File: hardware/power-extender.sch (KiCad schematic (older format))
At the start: 8 parts, among them J5 Conn_01x04_Male, J6 Conn_01x04_Male, U10 ADS1115IDGS, U9 ADS1115IDGS

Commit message: First draft
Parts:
- removed J5: Conn_01x04_Male, Connector_JST:JST_XH_B4B-XH-A_1x04_P2.50mm_Vertical, symbol Connector:Conn_01x04_Male
- added J5: RPI IFACE, Connector_JST:JST_XH_B5B-XH-A_1x05_P2.50mm_Vertical, symbol Connector:Conn_01x05_Male
- added J7: AUX DIGITAL, Connector_PinHeader_2.54mm:PinHeader_1x04_P2.54mm_Vertical, symbol Connector:Conn_01x04_Male
- added Q5, Q6: BSS138, Package_TO_SOT_SMD:SOT-23, symbol Transistor_FET:BSS138
- added R19: 1K, Resistor_SMD:R_0805_2012Metric, symbol Device:R
- added R20, R21: 10K, Resistor_SMD:R_0805_2012Metric, symbol Device:R
- added U11: PCA9557PW, Package_SO:TSSOP-16_4.4x5mm_P0.65mm, symbol CustomComponents:PCA9557PW
- C10, C9: footprint Capacitor_SMD:C_0201_0603Metric -> Capacitor_SMD:C_0805_2012Metric
- J6: value Conn_01x04_Male -> AUX ANALOG
- R17, R18: footprint Resistor_SMD:R_0201_0603Metric -> Resistor_SMD:R_0805_2012Metric
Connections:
- net labels added: +3V3, +5V, D0Z, D1, D2, D3
- net labels removed: VCC
- wire segments 36 -> 76
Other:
- note added: "ADDR: 0011000"
- note added: "Additional Analog Inputs"
- note added: "Low-Power Interfaces\nI2C Level Shifter"
- note added: "Relay Subsystem"
- moved on the sheet: C10, C9, J6, U10, U9

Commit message: Firnish schematic first version
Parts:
- added H1, H2, H3, H4: MountingHole, MountingHole:MountingHole_3.2mm_M3, symbol Mechanical:MountingHole
- added J8: IFACE PASS, Connector_JST:JST_XH_B5B-XH-A_1x05_P2.50mm_Vertical, symbol Connector:Conn_01x05_Male
- J5: value RPI IFACE -> IFACE RPI
- J6, J7: footprint Connector_PinHeader_2.54mm:PinHeader_1x04_P2.54mm_Vertical -> Connector_JST:JST_XH_B4B-XH-A_1x04_P2.50mm_Vertical
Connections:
- net +3V3: now also J8.2 (Pin_2)
- net +5V: now also J8.1 (Pin_1)
- net GND: now also J8.5 (Pin_5)
- net SDA3V3: now reaches J5.3 (Pin_3), Q5.2 (S), R17.2
- net SDA3V3: now also J8.3 (Pin_3)
- net SCL3V3: now reaches J5.4 (Pin_4), Q6.2 (S), R18.2
- net SCL3V3: now also J8.4 (Pin_4)
- net SCL renamed SCL5V
- net SDA renamed SDA5V
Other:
- moved on the sheet: C10, C9, J5, J6, J7, Q5, Q6, R17, R18, R19, R20, R21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

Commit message: checkpoint commit
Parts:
- added FID1, FID2, FID3: Fiducial, Fiducial:Fiducial_1mm_Mask2mm, symbol Mechanical:Fiducial
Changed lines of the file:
@@
 Wire Notes Line
 	8950 3300 8950 6000
+$Comp
+L Mechanical:Fiducial FID1
+U 1 1 60E092A2
+P 8350 2250
+F 0 "FID1" H 8435 2296 50  0000 L CNN
+F 1 "Fiducial" H 8435 2205 50  0000 L CNN
+F 2 "Fiducial:Fiducial_1mm_Mask2mm" H 8350 2250 50  0001 C CNN
+F 3 "~" H 8350 2250 50  0001 C CNN
+	1    8350 2250
+	1    0    0    -1
+$EndComp
+$Comp
+L Mechanical:Fiducial FID2
+U 1 1 60E0A4F4
+P 8350 2500
+F 0 "FID2" H 8435 2546 50  0000 L CNN
+F 1 "Fiducial" H 8435 2455 50  0000 L CNN
+F 2 "Fiducial:Fiducial_1mm_Mask2mm" H 8350 2500 50  0001 C CNN
+F 3 "~" H 8350 2500 50  0001 C CNN
+	1    8350 2500
+	1    0    0    -1
+$EndComp
+$Comp
+L Mechanical:Fiducial FID3
+U 1 1 60E11CA0
+P 8350 2750
+F 0 "FID3" H 8435 2796 50  0000 L CNN
+F 1 "Fiducial" H 8435 2705 50  0000 L CNN
+F 2 "Fiducial:Fiducial_1mm_Mask2mm" H 8350 2750 50  0001 C CNN
+F 3 "~" H 8350 2750 50  0001 C CNN
+	1    8350 2750
+	1    0    0    -1
+$EndComp
 $EndSCHEMATC

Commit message: relay layout checkpoint
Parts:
- renumbered C9 to C1, C10 to C2, J5 to J1, J8 to J2, J6 to J3, J7 to J4, Q5 to Q1, Q6 to Q2, R19 to R1, R17 to R2, R18 to R3, R20 to R4, R21 to R5, U9 to U1, U11 to U2, U10 to U3
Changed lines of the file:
@@
-$EndSheet
-$Sheet
-S 3250 4050 650  450
-U 60CBD6BF
-F0 "Relay-B" 50
-F1 "relay.sch" 50
-F2 "TRIGGER" I L 3250 4200 50
-F3 "VIOUT" O L 3250 4350 50
 $EndSheet
 $Sheet
@@
 U 60CBD7BB
 F0 "Relay-D" 50
-F1 "relay.sch" 50
+F1 "relay-mir.sch" 50
 F2 "TRIGGER" I L 1650 4200 50
 F3 "VIOUT" O L 1650 4350 50
 $EndSheet
 $Comp
-L Analog_ADC:ADS1115IDGS U9
+L Analog_ADC:ADS1115IDGS U1
 U 1 1 60CC7499
 P 3000 5450
-F 0 "U9" V 2550 5650 50  0000 C CNN
+F 0 "U1" V 2550 5650 50  0000 C CNN
 F 1 "ADS1115IDGS" V 2650 5850 50  0000 C CNN
 F 2 "Package_SO:TSSOP-10_3x3mm_P0.5mm" H 3000 4950 50  0001 C CNN
@@
 $EndComp
 $Comp
-L Device:C C9
+L Device:C C1
 U 1 1 60CF84D2
 P 3600 5600
-F 0 "C9" H 3715 5646 50  0000 L CNN
+F 0 "C1" H 3715 5646 50  0000 L CNN
 F 1 "100N" H 3715 5555 50  0000 L CNN
 F 2 "Capacitor_SMD:C_0805_2012Metric" H 3638 5450 50  0001 C CNN
@@
 $EndComp
 $Comp
-L power:GND #PWR0102
+L power:GND #PWR05
 U 1 1 60CFB3E8
 P 3600 5800
-F 0 "#PWR0102" H 3600 5550 50  0001 C CNN
+F 0 "#PWR05" H 3600 5550 50  0001 C CNN
 F 1 "GND" H 3605 5627 50  0000 C CNN
 F 2 "" H 3600 5800 50  0001 C CNN
@@
 $EndComp
 $Comp
-L power:GND #PWR0103
+L power:GND #PWR02
 U 1 1 60CFB7FE
 P 2600 5850
-F 0 "#PWR0103" H 2600 5600 50  0001 C CNN
+F 0 "#PWR02" H 2600 5600 50  0001 C CNN
 F 1 "GND" H 2605 5677 50  0000 C CNN
 F 2 "" H 2600 5850 50  0001 C CNN
@@
 Connection ~ 2600 5850
 $Comp
-L Analog_ADC:ADS1115IDGS U10
+L Analog_ADC:ADS1115IDGS U3
 U 1 1 60D01635
 P 6700 1850
-F 0 "U10" V 6250 2150 50  0000 C CNN
+F 0 "U3" V 6250 2150 50  0000 C CNN
 F 1 "ADS1115IDGS" V 6350 2300 50  0000 C CNN
 F 2 "Package_SO:TSSOP-10_3x3mm_P0.5mm" H 6700 1350 50  0001 C CNN
@@
 $EndComp
 $Comp
-L Device:C C10
+L Device:C C2
 U 1 1 60D016BD
 P 7300 2000
-F 0 "C10" H 7415 2046 50  0000 L CNN
+F 0 "C2" H 7415 2046 50  0000 L CNN
 F 1 "100N" H 7415 1955 50  0000 L CNN
 F 2 "Capacitor_SMD:C_0805_2012Metric" H 7338 1850 50  0001 C CNN
@@
 $EndComp
 $Comp
-L power:GND #PWR014
+L power:GND #PWR016
 U 1 1 60D016D1
 P 7300 2200
-F 0 "#PWR014" H 7300 1950 50  0001 C CNN
+F 0 "#PWR016" H 7300 1950 50  0001 C CNN
 F 1 "GND" H 7305 2027 50  0000 C CNN
 F 2 "" H 7300 2200 50  0001 C CNN
@@
 $EndComp
 $Comp
-L power:GND #PWR012
+L power:GND #PWR08
 U 1 1 60D016DB
 P 6300 1850
-F 0 "#PWR012" H 6300 1600 50  0001 C CNN
+F 0 "#PWR08" H 6300 1600 50  0001 C CNN
 F 1 "GND" H 6305 1677 50  0000 C CNN
 F 2 "" H 6300 1850 50  0001 C CNN
@@
 	6150 2250 6150 1850
 $Comp
-L power:GND #PWR09
+L power:GND #PWR010
 U 1 1 60D1D0AB
 P 6600 4450
-F 0 "#PWR09" H 6600 4200 50  0001 C CNN
+F 0 "#PWR010" H 6600 4200 50  0001 C CNN
 F 1 "GND" H 6605 4277 50  0000 C CNN
 F 2 "" H 6600 4450 50  0001 C CNN
@@
 ADDR: 1001001
 $Comp
-L Connector:Conn_01x04_Male J6
+L Connector:Conn_01x04_Male J3
 U 1 1 60D4012C
 P 7250 5250
-F 0 "J6" H 7358 5531 50  0000 C CNN
+F 0 "J3" H 7358 5531 50  0000 C CNN
 F 1 "AUX ANALOG" H 7358 5440 50  0000 C CNN
 F 2 "Connector_JST:JST_XH_B4B-XH-A_1x04_P2.50mm_Vertical" H 7250 5250 50  0001 C CNN
@@
 D2
 $Comp
-L CustomComponents:PCA9557PW U11
+L CustomComponents:PCA9557PW U2
 U 1 1 60C694D4
 P 3100 2600
-F 0 "U11" V 3300 3100 50  0000 L CNN
+F 0 "U2" V 3300 3100 50  0000 L CNN
 F 1 "PCA9557PW" V 3400 3100 50  0000 L CNN
 F 2 "Package_SO:TSSOP-16_4.4x5mm_P0.65mm" H 3100 2600 50  0001 C CNN
@@
 $EndComp
 $Comp
-L power:GND #PWR015
+L power:GND #PWR01
 U 1 1 60C8F4E4
 P 2500 2650
-F 0 "#PWR015" H 2500 2400 50  0001 C CNN
+F 0 "#PWR01" H 2500 2400 50  0001 C CNN
 F 1 "GND" H 2505 2477 50  0000 C CNN
 F 2 "" H 2500 2650 50  0001 C CNN
@@
 SCL5V
 $Comp
-L Device:R R19
+L Device:R R1
 U 1 1 60C9DB37
 P 3150 1650
-F 0 "R19" H 3220 1696 50  0000 L CNN
+F 0 "R1" H 3220 1696 50  0000 L CNN
 F 1 "1K" H 3220 1605 50  0000 L CNN
 F 2 "Resistor_SMD:R_0805_2012Metric" V 3080 1650 50  0001 C CNN
@@
 	2750 3350 2750 3100
 $Comp
-L Connector:Conn_01x04_Male J7
+L Connector:Conn_01x04_Male J4
 U 1 1 60C77624
 P 7950 5250
-F 0 "J7" H 8058 5531 50  0000 C CNN
+F 0 "J4" H 8058 5531 50  0000 C CNN
 F 1 "AUX DIGITAL" H 8058 5440 50  0000 C CNN
 F 2 "Connector_JST:JST_XH_B4B-XH-A_1x04_P2.50mm_Vertical" H 7950 5250 50  0001 C CNN
@@
 D3
 $Comp
-L Connector:Conn_01x05_Male J5
+L Connector:Conn_01x05_Male J1
 U 1 1 60CC2070
 P 6300 4150
-F 0 "J5" H 6408 4531 50  0000 C CNN
+F 0 "J1" H 6408 4531 50  0000 C CNN
 F 1 "IFACE RPI" H 6300 4450 50  0000 C CNN
 F 2 "Connector_JST:JST_XH_B5B-XH-A_1x05_P2.50mm_Vertical" H 6300 4150 50  0001 C CNN
@@
 $EndComp
 $Comp
-L power:+5V #PWR07
+L power:+5V #PWR09
 U 1 1 60CC5D0E
 P 6600 3650
-F 0 "#PWR07" H 6600 3500 50  0001 C CNN
+F 0 "#PWR09" H 6600 3500 50  0001 C CNN
 F 1 "+5V" H 6615 3823 50  0000 C CNN
 F 2 "" H 6600 3650 50  0001 C CNN
@@
 	6500 4050 6850 4050
 $Comp
-L power:+5V #PWR013
+L power:+5V #PWR015
 U 1 1 60CCF760
 P 7300 1850
-F 0 "#PWR013" H 7300 1700 50  0001 C CNN
+F 0 "#PWR015" H 7300 1700 50  0001 C CNN
 F 1 "+5V" H 7315 2023 50  0000 C CNN
 F 2 "" H 7300 1850 50  0001 C CNN
@@
 Connection ~ 7300 1850
 $Comp
-L power:+5V #PWR05
+L power:+5V #PWR06
 U 1 1 60CD11FC
 P 3700 2550
-F 0 "#PWR05" H 3700 2400 50  0001 C CNN
+F 0 "#PWR06" H 3700 2400 50  0001 C CNN
 F 1 "+5V" H 3715 2723 50  0000 C CNN
 F 2 "" H 3700 2550 50  0001 C CNN
@@
 $EndComp
 $Comp
-L power:+5V #PWR02
+L power:+5V #PWR03
 U 1 1 60CD1663
 P 3150 1500
-F 0 "#PWR02" H 3150 1350 50  0001 C CNN
+F 0 "#PWR03" H 3150 1350 50  0001 C CNN
 F 1 "+5V" H 3165 1673 50  0000 C CNN
 F 2 "" H 3150 1500 50  0001 C CNN
@@
 $EndComp
 $Comp
-L power:+5V #PWR03
+L power:+5V #PWR04
 U 1 1 60CD2867
 P 3600 5450
-F 0 "#PWR03" H 3600 5300 50  0001 C CNN
+F 0 "#PWR04" H 3600 5300 50  0001 C CNN
 F 1 "+5V" H 3615 5623 50  0000 C CNN
 F 2 "" H 3600 5450 50  0001 C CNN
@@
 	6850 3650 6850 4050
 $Comp
-L power:+3V3 #PWR010
+L power:+3V3 #PWR013
 U 1 1 60D39B7C
 P 6850 3650
-F 0 "#PWR010" H 6850 3500 50  0001 C CNN
+F 0 "#PWR013" H 6850 3500 50  0001 C CNN
 F 1 "+3V3" H 6865 3823 50  0000 C CNN
 F 2 "" H 6850 3650 50  0001 C CNN
@@
 	8950 3300 5950 3300
 $Comp
-L power:+5V #PWR011
+L power:+5V #PWR07
 U 1 1 60DA5585
 P 6150 1850
-F 0 "#PWR011" H 6150 1700 50  0001 C CNN
+F 0 "#PWR07" H 6150 1700 50  0001 C CNN
 F 1 "+5V" H 6165 2023 50  0000 C CNN
 F 2 "" H 6150 1850 50  0001 C CNN
@@
 	7700 4550 7300 4550
 $Comp
-L Transistor_FET:BSS138 Q6
+L Transistor_FET:BSS138 Q2
 U 1 1 60C91A55
 P 7900 4450
-F 0 "Q6" V 8149 4450 50  0000 C CNN
+F 0 "Q2" V 8149 4450 50  0000 C CNN
 F 1 "BSS138" V 8240 4450 50  0000 C CNN
 F 2 "Package_TO_SOT_SMD:SOT-23" H 8100 4375 50  0001 L CIN
@@
 	7650 3850 7650 3650
 $Comp
-L power:+5V #PWR016
+L power:+5V #PWR017
 U 1 1 60D19EDA
 P 8100 3650
-F 0 "#PWR016" H 8100 3500 50  0001 C CNN
+F 0 "#PWR017" H 8100 3500 50  0001 C CNN
 F 1 "+5V" H 8115 3823 50  0000 C CNN
 F 2 "" H 8100 3650 50  0001 C CNN
@@
 	8500 4550 8400 4550
 $Comp
-L Device:R R20
+L Device:R R4
 U 1 1 60CE19B5
 P 8100 3800
-F 0 "R20" H 8170 3846 50  0000 L CNN
+F 0 "R4" H 8170 3846 50  0000 L CNN
 F 1 "10K" H 8170 3755 50  0000 L CNN
 F 2 "Resistor_SMD:R_0805_2012Metric" V 8030 3800 50  0001 C CNN
@@
 $EndComp
 $Comp
-L Device:R R17
+L Device:R R2
 U 1 1 60CE147E
 P 7000 3800
-F 0 "R17" H 7070 3846 50  0000 L CNN
+F 0 "R2" H 7070 3846 50  0000 L CNN
 F 1 "10K" H 7070 3755 50  0000 L CNN
 F 2 "Resistor_SMD:R_0805_2012Metric" V 6930 3800 50  0001 C CNN
@@
 $EndComp
 $Comp
-L Device:R R21
+L Device:R R5
 U 1 1 60CE0F55
 P 8400 3800
-F 0 "R21" H 8470 3846 50  0000 L CNN
+F 0 "R5" H 8470 3846 50  0000 L CNN
 F 1 "10K" H 8470 3755 50  0000 L CNN
 F 2 "Resistor_SMD:R_0805_2012Metric" V 8330 3800 50  0001 C CNN
@@
 $EndComp
 $Comp
-L Transistor_FET:BSS138 Q5
+L Transistor_FET:BSS138 Q1
 U 1 1 60C8F9B0
 P 7650 4050
-F 0 "Q5" V 7899 4050 50  0000 C CNN
+F 0 "Q1" V 7899 4050 50  0000 C CNN
 F 1 "BSS138" V 7990 4050 50  0000 C CNN
 F 2 "Package_TO_SOT_SMD:SOT-23" H 7850 3975 50  0001 L CIN
@@
 $EndComp
 $Comp
-L Device:R R18
+L Device:R R3
 U 1 1 60C97FA7
 P 7300 3800
-F 0 "R18" H 7370 3846 50  0000 L CNN
+F 0 "R3" H 7370 3846 50  0000 L CNN
 F 1 "10K" H 7370 3755 50  0000 L CNN
 F 2 "Resistor_SMD:R_0805_2012Metric" V 7230 3800 50  0001 C CNN
@@
 Connection ~ 6850 3650
 $Comp
-L Connector:Conn_01x05_Male J8
+L Connector:Conn_01x05_Male J2
 U 1 1 60D7FCBF
 P 6300 5350
-F 0 "J8" H 6408 5731 50  0000 C CNN
+F 0 "J2" H 6408 5731 50  0000 C CNN
 F 1 "IFACE PASS" H 6250 5650 50  0000 C CNN
 F 2 "Connector_JST:JST_XH_B5B-XH-A_1x05_P2.50mm_Vertical" H 6300 5350 50  0001 C CNN
@@
 $EndComp
 $Comp
-L power:GND #PWR022
+L power:GND #PWR012
 U 1 1 60D869C1
 P 6600 5650
-F 0 "#PWR022" H 6600 5400 50  0001 C CNN
+F 0 "#PWR012" H 6600 5400 50  0001 C CNN
 F 1 "GND" H 6605 5477 50  0000 C CNN
 F 2 "" H 6600 5650 50  0001 C CNN
@@
 $EndComp
 $Comp
-L power:+5V #PWR021
+L power:+5V #PWR011
 U 1 1 60D87009
 P 6600 5050
-F 0 "#PWR021" H 6600 4900 50  0001 C CNN
+F 0 "#PWR011" H 6600 4900 50  0001 C CNN
 F 1 "+5V" H 6615 5223 50  0000 C CNN
 F 2 "" H 6600 5050 50  0001 C CNN
@@
 $EndComp
 $Comp
-L power:+3V3 #PWR023
+L power:+3V3 #PWR014
 U 1 1 60D87886
 P 6850 5050
-F 0 "#PWR023" H 6850 4900 50  0001 C CNN
+F 0 "#PWR014" H 6850 4900 50  0001 C CNN
 F 1 "+3V3" H 6865 5223 50  0000 C CNN
 F 2 "" H 6850 5050 50  0001 C CNN
@@
 	1    0    0    -1
 $EndComp
+$Sheet
+S 3250 4050 650  450
+U 60CBD6BF
+F0 "Relay-B" 50
+F1 "relay-mir.sch" 50
+F2 "TRIGGER" I L 3250 4200 50
+F3 "VIOUT" O L 3250 4350 50
+$EndSheet
 $EndSCHEMATC

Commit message: traces done
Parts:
- removed H3, H4: MountingHole, MountingHole:MountingHole_3.2mm_M3, symbol Mechanical:MountingHole
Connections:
- net D0Z: now also J4.4 (Pin_4); no longer J4.1 (Pin_1)
- net D1: now also J4.3 (Pin_3); no longer J4.2 (Pin_2)
- net D2: now also J4.2 (Pin_2); no longer J4.3 (Pin_3)
- net D3: now also J4.1 (Pin_1); no longer J4.4 (Pin_4)
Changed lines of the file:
@@
 	1    0    0    -1
 $EndComp
+Text GLabel 8150 5350 2    50   Input ~ 0
+D1
 Text GLabel 8150 5250 2    50   Input ~ 0
-D1
-Text GLabel 8150 5350 2    50   Input ~ 0
 D2
 Text GLabel 3350 2100 1    50   BiDi ~ 0
@@
 	1    0    0    -1
 $EndComp
-Text GLabel 8150 5450 2    50   Input ~ 0
+Text GLabel 8150 5150 2    50   Input ~ 0
 D3
 $Comp
@@
 	1    0    0    -1
 $EndComp
-$Comp
-L Mechanical:MountingHole H3
-U 1 1 60DEB62A
-P 8350 1750
-F 0 "H3" H 8450 1796 50  0000 L CNN
-F 1 "MountingHole" H 8450 1705 50  0000 L CNN
-F 2 "MountingHole:MountingHole_3.2mm_M3" H 8350 1750 50  0001 C CNN
-F 3 "~" H 8350 1750 50  0001 C CNN
-	1    8350 1750
-	1    0    0    -1
-$EndComp
-$Comp
-L Mechanical:MountingHole H4
-U 1 1 60DEBDBB
-P 8350 2000
-F 0 "H4" H 8450 2046 50  0000 L CNN
-F 1 "MountingHole" H 8450 1955 50  0000 L CNN
-F 2 "MountingHole:MountingHole_3.2mm_M3" H 8350 2000 50  0001 C CNN
-F 3 "~" H 8350 2000 50  0001 C CNN
-	1    8350 2000
-	1    0    0    -1
-$EndComp
 Wire Wire Line
 	6500 4150 6850 4150
@@
 Text GLabel 6500 5350 2    50   BiDi ~ 0
 SDA3V3
-Text GLabel 8150 5150 2    50   Input ~ 0
+Text GLabel 8150 5450 2    50   Input ~ 0
 D0Z
 Wire Wire Line

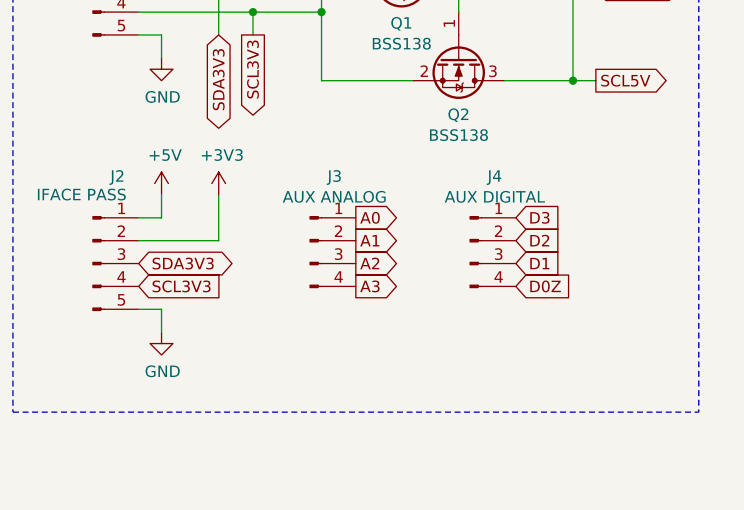
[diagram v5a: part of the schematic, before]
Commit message: Add bjt pulldown, prepare for export
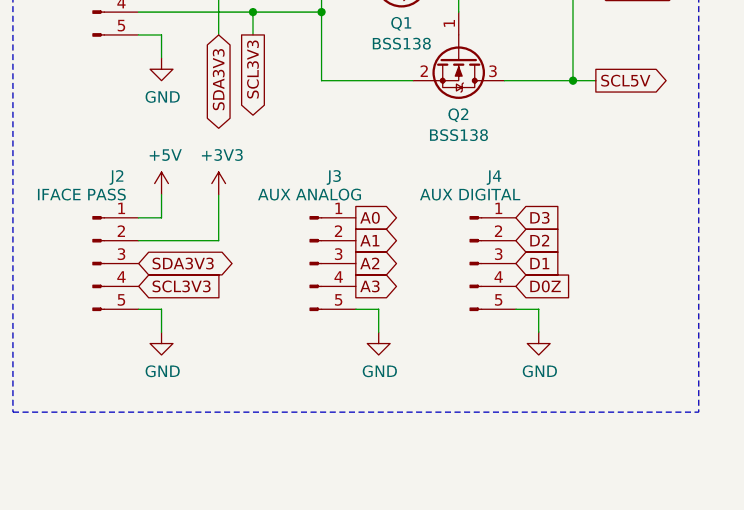
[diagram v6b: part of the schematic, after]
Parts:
- removed J3: AUX ANALOG, Connector_JST:JST_XH_B4B-XH-A_1x04_P2.50mm_Vertical, symbol Connector:Conn_01x04_Male
- removed J4: AUX DIGITAL, Connector_JST:JST_XH_B4B-XH-A_1x04_P2.50mm_Vertical, symbol Connector:Conn_01x04_Male
- added J3: AUX ANALOG, Connector_JST:JST_XH_B5B-XH-A_1x05_P2.50mm_Vertical, symbol Connector:Conn_01x05_Male
- added J4: AUX DIGITAL, Connector_JST:JST_XH_B5B-XH-A_1x05_P2.50mm_Vertical, symbol Connector:Conn_01x05_Male
- C1, C2: Description / Value (none) -> CAP CER 100NF MAX. 5% MIN. 10V 0805 SMD; Distributor (none) -> Any; Distributor part # (none) -> TBD; Manufacturer (none) -> TBD; Manufacturer Part # (none) -> TBD; Package / Footprint (none) -> 0805; Type (none) -> SMD
- FID1, FID2, FID3: Description / Value (none) -> FIDUCIAL MARK; Distributor (none) -> N/A; Distributor part # (none) -> N/A; Manufacturer (none) -> N/A; Manufacturer Part # (none) -> N/A; Package / Footprint (none) -> N/A; Type (none) -> N/A
- H1, H2: Description / Value (none) -> MOUNTING HOLE 3.2MM; Distributor (none) -> N/A; Distributor part # (none) -> N/A; Manufacturer (none) -> N/A; Manufacturer Part # (none) -> N/A; Package / Footprint (none) -> N/A; Type (none) -> N/A
- J1, J2: Description / Value (none) -> CONN JST-XH-2.50MM VERTICAL MALE HEADER 5 PIN; Distributor (none) -> Any; Distributor part # (none) -> TBD; Manufacturer (none) -> TBD; Manufacturer Part # (none) -> TBD; Package / Footprint (none) -> Through-Hole; Type (none) -> THT
- Q1, Q2: Description / Value (none) -> MOSFET N-CH SOT-23-3; Distributor (none) -> LCSC; Distributor part # (none) -> C112239; Manufacturer (none) -> Shikues; Manufacturer Part # (none) -> BSS138; Package / Footprint (none) -> SOT-23-3; Type (none) -> SMD
- R1: Description / Value (none) -> RES 1K OHM MAX. 1% MIN. 1/8W 0805 SMD; Distributor (none) -> Any; Distributor part # (none) -> TBD; Manufacturer (none) -> TBD; Manufacturer Part # (none) -> TBD; Package / Footprint (none) -> 0805; Type (none) -> SMD
- R2, R3, R4, R5: Description / Value (none) -> RES 10K OHM MAX. 1% MIN. 1/8W 0805 SMD; Distributor (none) -> Any; Distributor part # (none) -> TBD; Manufacturer (none) -> TBD; Manufacturer Part # (none) -> TBD; Package / Footprint (none) -> 0805; Type (none) -> SMD
- U1, U3: Description / Value (none) -> IC I2C 4 CH ADC VSSOP-10; Distributor (none) -> LCSC; Distributor part # (none) -> C37593; Manufacturer (none) -> Texas Instruments; Manufacturer Part # (none) -> ADS1115IDGSR; Package / Footprint (none) -> VSSOP-10; Type (none) -> SMD
- U2: Description / Value (none) -> IC I2C 8 CH IO EXP TSSOP-16; Distributor (none) -> LCSC; Distributor part # (none) -> C141380; Manufacturer (none) -> NXP Semicon; Manufacturer Part # (none) -> PCA9557PW,118; Package / Footprint (none) -> TSSOP-16; Type (none) -> SMD
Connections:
- net A0: now also J3.1 (Pin_1)
- net A1: now also J3.2 (Pin_2)
- net A2: now also J3.3 (Pin_3)
- net A3: now also J3.4 (Pin_4)
- net D0Z: now also J4.4 (Pin_4)
- net D1: now also J4.3 (Pin_3)
- net D2: now also J4.2 (Pin_2)
- net D3: now also J4.1 (Pin_1)
- net GND: now also J3.5 (Pin_5), J4.5 (Pin_5)

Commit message: Add rev 1.1 fabrication files
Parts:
- J1, J2, J3, J4: footprint Connector_JST:JST_XH_B5B-XH-A_1x05_P2.50mm_Vertical -> CustomComponents:JST_XH_B5B-XH-A_1x05_P2.54mm_Vertical
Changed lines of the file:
@@
 F 0 "J1" H 6408 4531 50  0000 C CNN
 F 1 "IFACE RPI" H 6300 4450 50  0000 C CNN
-F 2 "Connector_JST:JST_XH_B5B-XH-A_1x05_P2.50mm_Vertical" H 6300 4150 50  0001 C CNN
+F 2 "CustomComponents:JST_XH_B5B-XH-A_1x05_P2.54mm_Vertical" H 6300 4150 50  0001 C CNN
 F 3 "~" H 6300 4150 50  0001 C CNN
 F 4 "CONN JST-XH-2.50MM VERTICAL MALE HEADER 5 PIN" H 6300 4150 50  0001 C CNN "Description / Value"
@@
 F 0 "J2" H 6408 5731 50  0000 C CNN
 F 1 "IFACE PASS" H 6250 5650 50  0000 C CNN
-F 2 "Connector_JST:JST_XH_B5B-XH-A_1x05_P2.50mm_Vertical" H 6300 5350 50  0001 C CNN
+F 2 "CustomComponents:JST_XH_B5B-XH-A_1x05_P2.54mm_Vertical" H 6300 5350 50  0001 C CNN
 F 3 "~" H 6300 5350 50  0001 C CNN
 F 4 "CONN JST-XH-2.50MM VERTICAL MALE HEADER 5 PIN" H 6300 5350 50  0001 C CNN "Description / Value"
@@
 F 0 "J3" H 7358 5731 50  0000 C CNN
 F 1 "AUX ANALOG" H 7250 5650 50  0000 C CNN
-F 2 "Connector_JST:JST_XH_B5B-XH-A_1x05_P2.50mm_Vertical" H 7250 5350 50  0001 C CNN
+F 2 "CustomComponents:JST_XH_B5B-XH-A_1x05_P2.54mm_Vertical" H 7250 5350 50  0001 C CNN
 F 3 "~" H 7250 5350 50  0001 C CNN
 F 4 "CONN JST-XH-2.50MM VERTICAL MALE HEADER 5 PIN" H 7250 5350 50  0001 C CNN "Description / Value"
@@
 F 0 "J4" H 8058 5731 50  0000 C CNN
 F 1 "AUX DIGITAL" H 7950 5650 50  0000 C CNN
-F 2 "Connector_JST:JST_XH_B5B-XH-A_1x05_P2.50mm_Vertical" H 7950 5350 50  0001 C CNN
+F 2 "CustomComponents:JST_XH_B5B-XH-A_1x05_P2.54mm_Vertical" H 7950 5350 50  0001 C CNN
 F 3 "~" H 7950 5350 50  0001 C CNN
 F 4 "CONN JST-XH PITCH-2.50MM VERTICAL MALE HEADER 5 PIN" H 7950 5350 50  0001 C CNN "Description / Value"
